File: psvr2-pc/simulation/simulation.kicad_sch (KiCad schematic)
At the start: 32 parts, among them Q1 PMOS, Q2 PMOS, Q3 NPN, Q4 PMOS, Q5 PMOS, Q6 NPN, Q8 PMOS

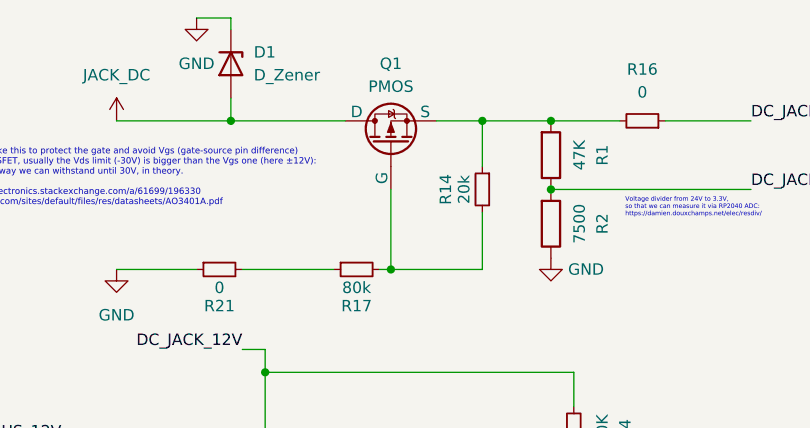
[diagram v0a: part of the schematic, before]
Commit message: Start to learn how to add the SPICE model parameters to simulate a TVS voltage protection diode array and confirm it works, not working yet, getting there.
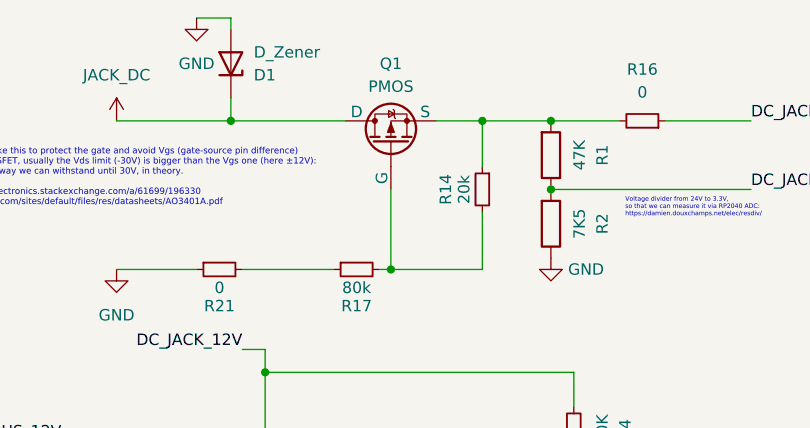
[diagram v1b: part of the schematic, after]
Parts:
- R2: value 7500 -> 7K5
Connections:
- net GND: now also D1.2 (A); no longer D1.1 (K)
- net JACK_DC: now also D1.1 (K); no longer D1.2 (A)
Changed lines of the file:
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@@
 			)
 		)
-		(property "Value" "7500"
+		(property "Value" "7K5"
 			(at 120.015 33.02 90)
 			(effects
@@
 		(lib_id "Device:D_Zener")
 		(at 81.28 15.24 270)
-		(unit 1)
-		(exclude_from_sim no)
-		(in_bom yes)
-		(on_board yes)
-		(dnp no)
-		(fields_autoplaced yes)
+		(mirror x)
+		(unit 1)
+		(exclude_from_sim no)
+		(in_bom yes)
+		(on_board yes)
+		(dnp no)
 		(property "Reference" "D1"
-			(at 83.82 13.9699 90)
+			(at 83.82 16.5101 90)
 			(effects
 				(font
@@
 		)
 		(property "Value" "D_Zener"
-			(at 83.82 16.5099 90)
+			(at 83.82 13.9701 90)
 			(effects
 				(font
@@
 			)
 		)
-		(property "Datasheet" "~"
+		(property "Datasheet" "https://protekdevices.com/wp-content/uploads/datasheets/psm712.pdf"
 			(at 81.28 15.24 0)
 			(effects
@@
 			)
 		)
-		(property "Description" "Zener diode"
+		(property "Description" "TVS ARRAY"
 			(at 81.28 15.24 0)
 			(effects
@@
 			)
 		)
-		(property "Sim.Pins" "1=K, 2=A"
+		(property "Sim.Pins" "1=A 2=K"
 			(at 81.28 15.24 0)
 			(effects
+				(font
+					(size 1.27 1.27)
+				)
+				(hide yes)
+			)
+		)
+		(property "Sim.Params" "m=0.33 is=1e-13 rs=0.40 n=1 tt=1E vj=.6 cjp=1.23e-10 eg=1.11 bv=13.3 ibv=0.001"
+			(at 81.28 15.24 0)
+			(effects

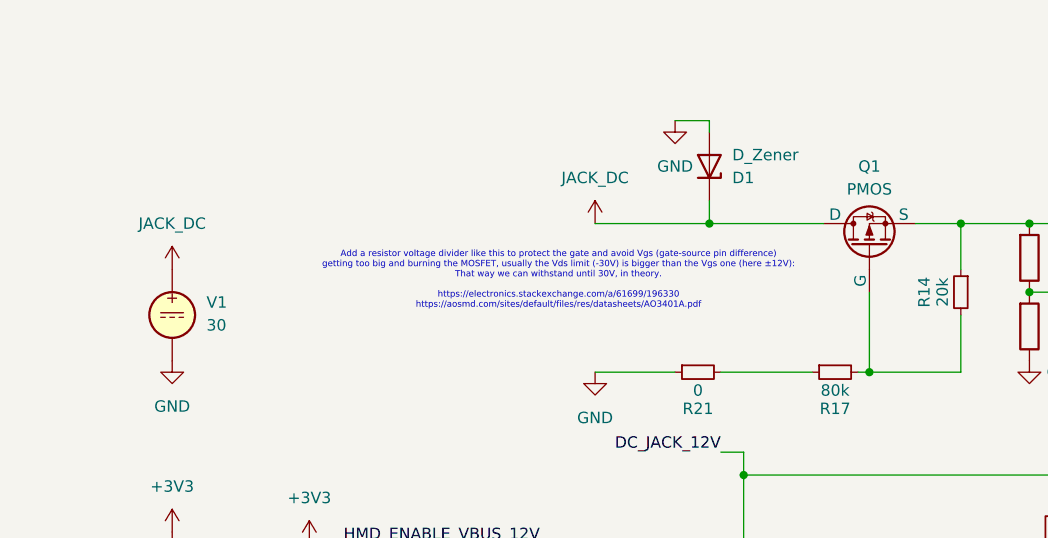
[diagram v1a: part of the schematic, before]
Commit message: Mess around a bit more with the simulation. can't say I really know what's wrong or why the simulation isn't clamping anything. Worth studying more in the future.
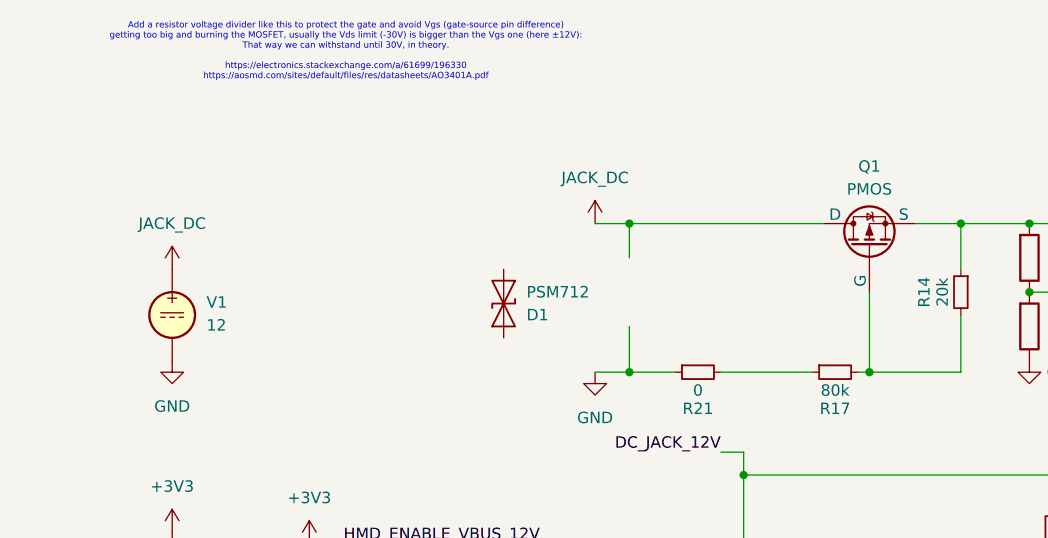
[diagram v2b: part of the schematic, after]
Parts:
- removed D1: D_Zener, symbol Device:D_Zener
- added D1: PSM712, Diode_SMD:D_SMA, symbol Diode:SMAJ12CA
- V1: value 30 -> 12

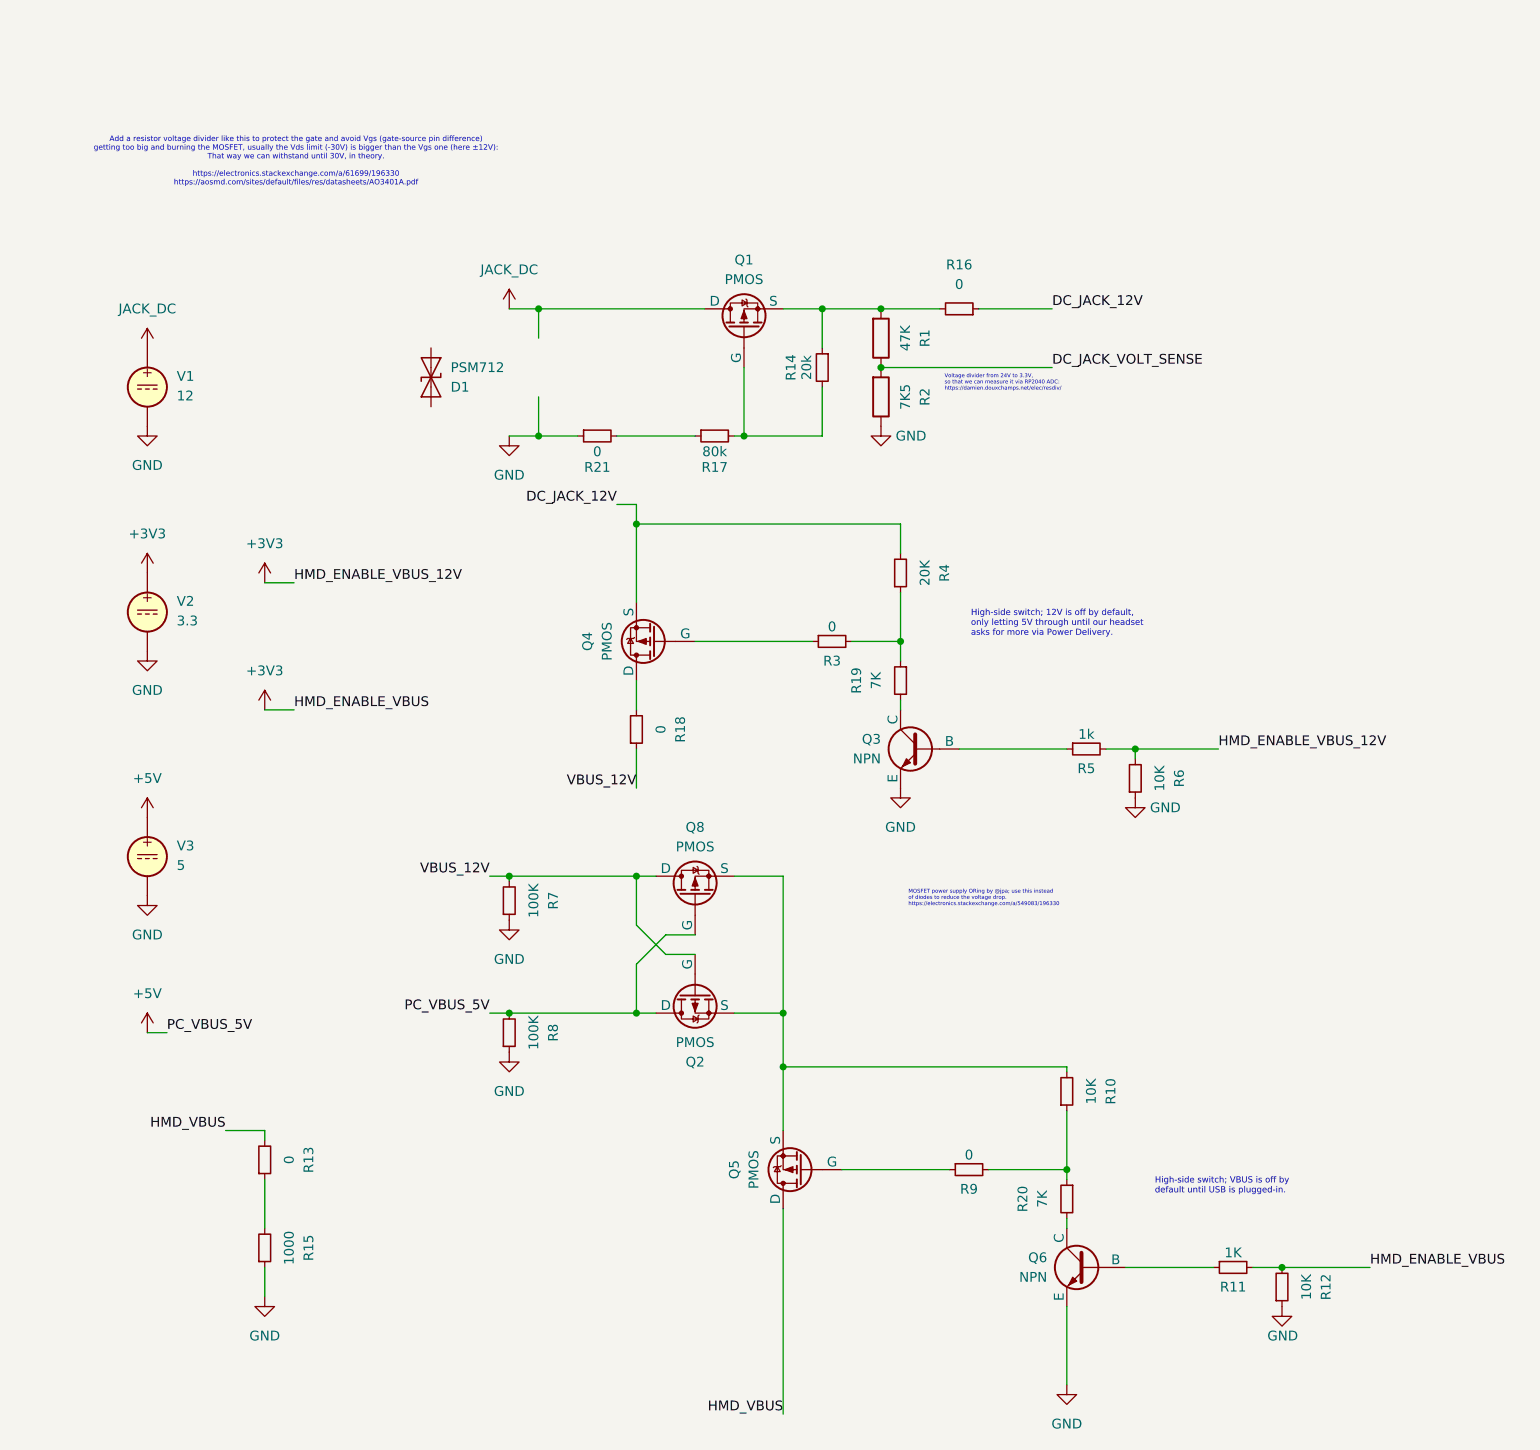
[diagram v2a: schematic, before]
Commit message: Fix the power gating simulation again, remove all the custom properties and impedance from the 12V power source. Switch from the generic NPN transistors to MMBT2222A.
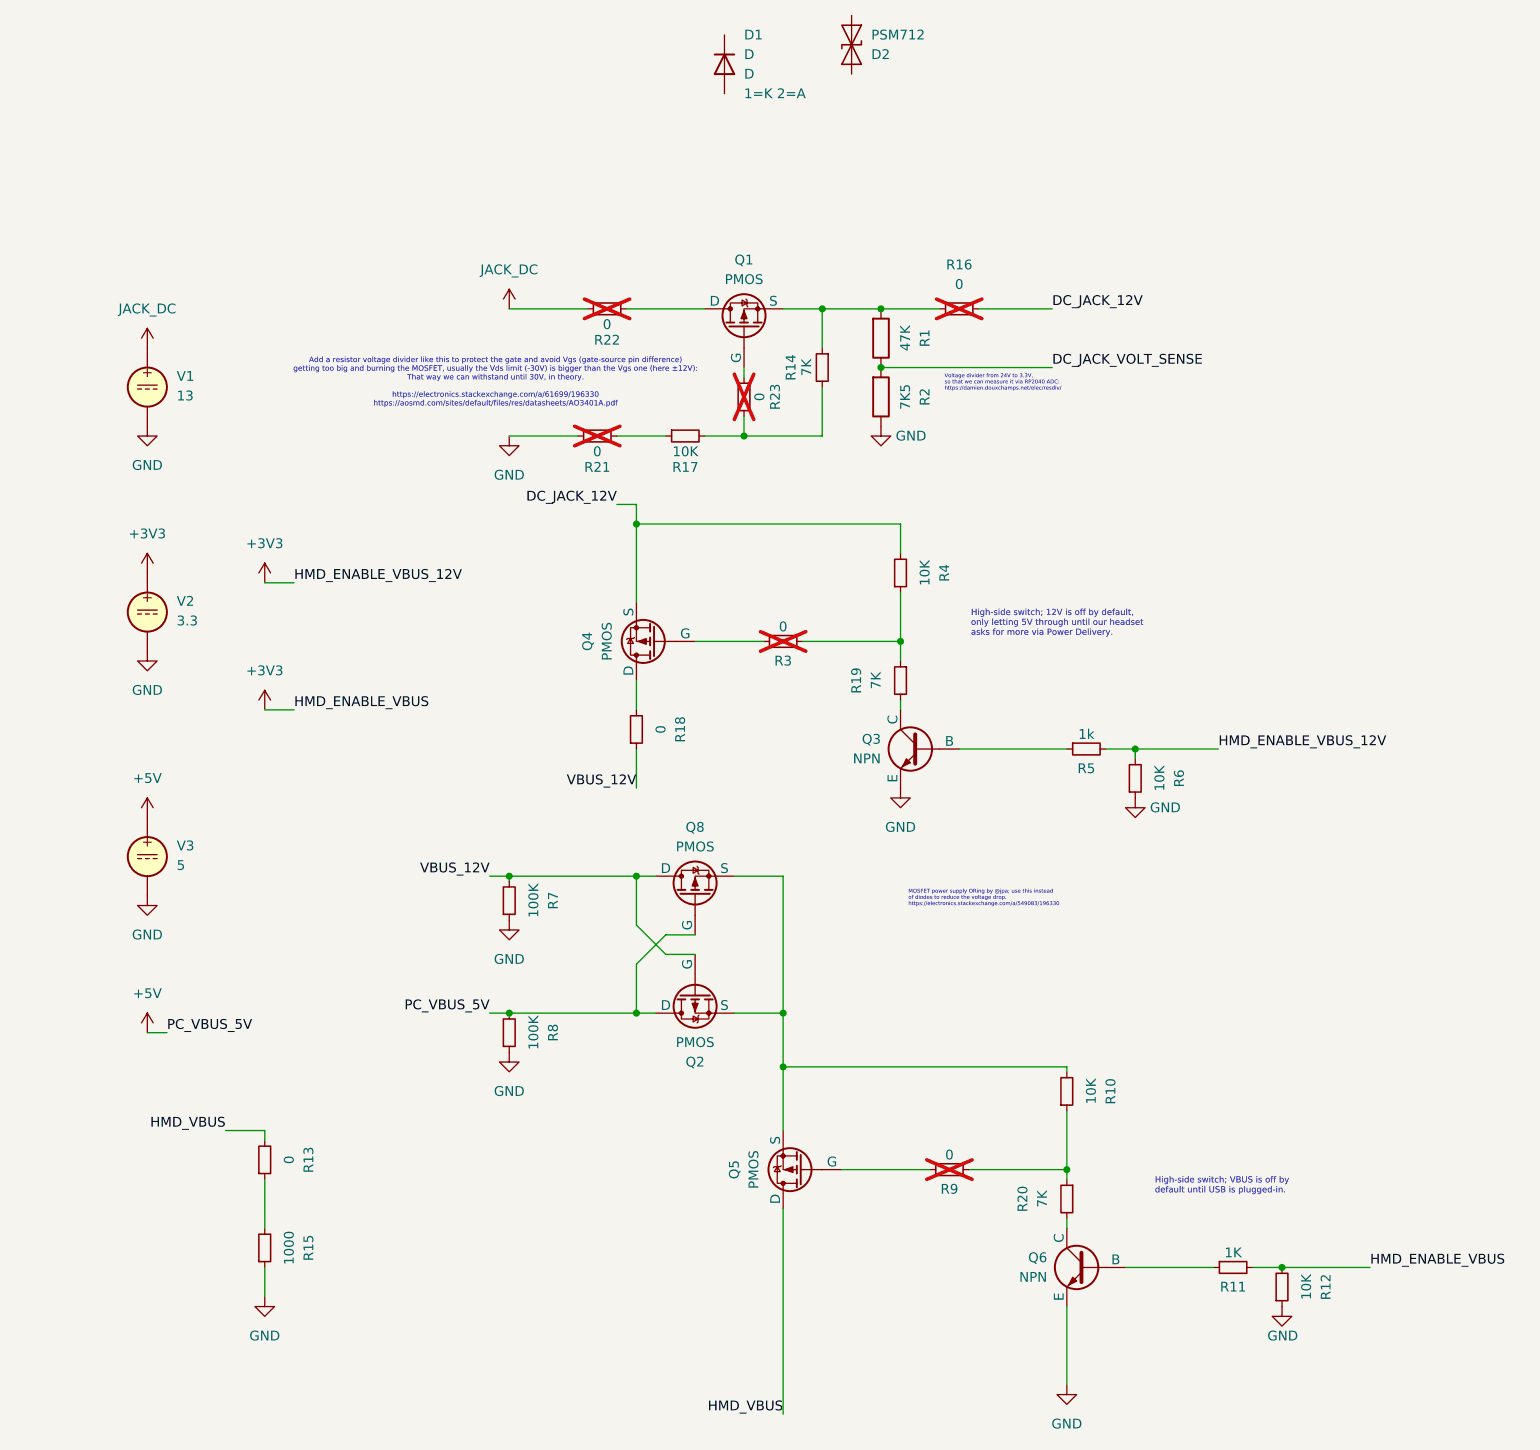
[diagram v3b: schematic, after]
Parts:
- removed D1: PSM712, Diode_SMD:D_SMA, symbol Diode:SMAJ12CA
- added D1: D, symbol Simulation_SPICE:D
- added D2: PSM712, Diode_SMD:D_SMA, symbol Diode:SMAJ12CA
- added R22, R23: 0, Resistor_SMD:R_0805_2012Metric, symbol Device:R_Small
- R14: value 20k -> 7K
- R16, R21, R3, R9: now not fitted
- R17: value 80k -> 10K
- R4: value 20K -> 10K
- V1: value 12 -> 13
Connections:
- net JACK_DC: now also R22.1; no longer Q1.1 (D)
- net at R14.2, R17.2: now also R23.1; no longer Q1.2 (G)
- new net: Q1.1 (D), R22.2
- new net: Q1.2 (G), R23.2
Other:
- moved on the sheet: R17

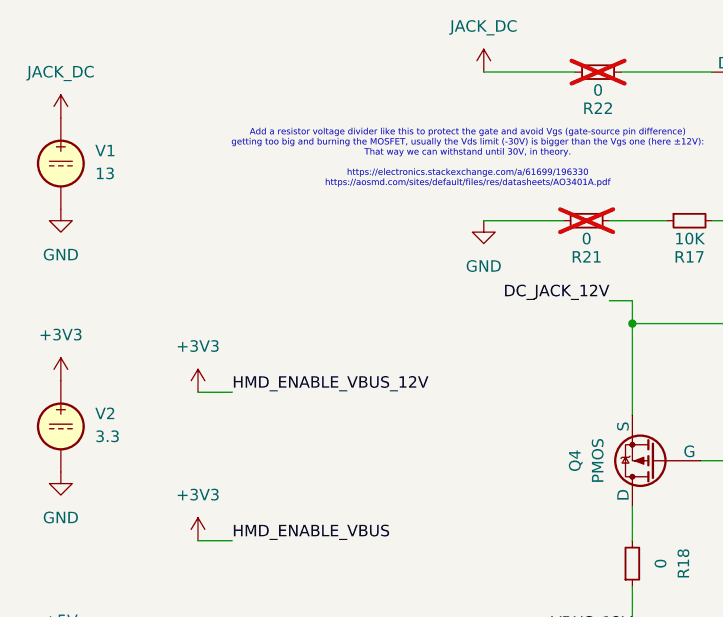
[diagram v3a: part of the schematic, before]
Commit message: Use relative paths for the SPICE symbols, store them in the git repository. Just to make things easier. Explain how to toggle pins, for those struggling like me.
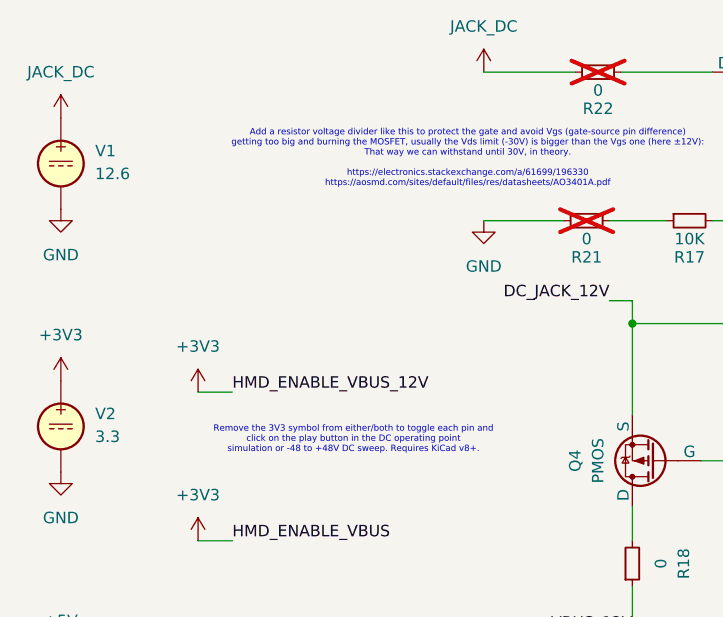
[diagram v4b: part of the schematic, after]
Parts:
- V1: value 13 -> 12.6
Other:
- note added: "Remove the 3V3 symbol from either/both to toggle each pin and click on the play button in the DC operating point simulation or -48 to +48V DC sweep. Requires KiCad v8+."
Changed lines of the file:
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@@
 		)
 	)
+	(text "Remove the 3V3 symbol from either/both to toggle each pin and\nclick on the play button in the DC operating point\nsimulation or -48 to +48V DC sweep. Requires KiCad v8+."
+		(exclude_from_sim no)
+		(at 54.102 62.484 0)
+		(effects
+			(font
+				(size 0.7 0.7)
+			)
+		)
+	)
 	(text "Voltage divider from 24V to 3.3V,\nso that we can measure it via RP2040 ADC:\nhttps://damien.douxchamps.net/elec/resdiv/"
 		(exclude_from_sim no)
@@
 			)
 		)
-		(property "Value" "13"
+		(property "Value" "12.6"
 			(at 25.4 32.8901 0)
 			(effects
@@
 			)
 		)
-		(property "Sim.Library" "C:\\Users\\Usuario\\Downloads\\MMBT2222A.txt"
+		(property "Sim.Library" "./_spice_component_models/MMBT2222A.txt"
 			(at 143.51 146.05 0)
 			(effects
@@
 			)
 		)
-		(property "Sim.Library" "C:\\Users\\Usuario\\Downloads\\AO3401A.mod"
+		(property "Sim.Library" "./_spice_component_models/AO3401A.mod"
 			(at 106.68 133.35 0)
 			(effects
@@
 			)
 		)
-		(property "Sim.Library" "C:\\Users\\Usuario\\Downloads\\AO3401A.mod"
+		(property "Sim.Library" "./_spice_component_models/AO3401A.mod"
 			(at 92.71 97.79 90)
 			(effects
@@
 			)
 		)
-		(property "Sim.Library" "C:\\Users\\Usuario\\Downloads\\AO3401A.mod"
+		(property "Sim.Library" "./_spice_component_models/AO3401A.mod"
 			(at 87.63 64.77 0)
 			(effects
@@
 			)
 		)
-		(property "Sim.Library" "C:\\Users\\Usuario\\Downloads\\MMBT2222A.txt"
+		(property "Sim.Library" "./_spice_component_models/MMBT2222A.txt"
 			(at 121.92 78.74 0)
 			(effects
@@
 			)
 		)
-		(property "Sim.Library" "C:\\Users\\Usuario\\Downloads\\AO3401A.mod"
+		(property "Sim.Library" "./_spice_component_models/AO3401A.mod"
 			(at 99.06 24.13 0)
 			(effects
@@
 			)
 		)
-		(property "Sim.Library" "C:\\Users\\Usuario\\Downloads\\AO3401A.mod"
+		(property "Sim.Library" "./_spice_component_models/AO3401A.mod"
 			(at 92.71 110.49 0)
 			(effects

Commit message: Update the resistor sizes to make them cheap. Use 51K/8K2 for the 24V to 3.3V divider. Use 6K8 instead of 7K. Update the simulation, seems to still work fine. Add the LCSC Part # to the NPN transistor and remove obsolete C part numbers from resistors and capacitors that now had the wrong size. Mark the M4 and SMT assembly holes as not-in-schematic and not in position file, name them to avoid auto-generated names which cause errors in  the JLC ordering process.
Currently available resistor sizes as basic parts:
5.1kΩ 6.8kΩ 8.2kΩ
47kΩ 51kΩ 68kΩ
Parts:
- R1: value 47K -> 51K
- R14, R19, R20: value 7K -> 6K8
- R2: value 7K5 -> 8K2
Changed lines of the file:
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@@
 			)
 		)
-		(property "Value" "7K5"
+		(property "Value" "8K2"
 			(at 120.015 33.02 90)
 			(effects
@@
 			)
 		)
-		(property "Value" "7K"
+		(property "Value" "6K8"
 			(at 107.188 29.21 90)
 			(effects
@@
 			)
 		)
-		(property "Value" "7K"
+		(property "Value" "6K8"
 			(at 137.795 137.16 90)
 			(effects
@@
 			)
 		)
-		(property "Value" "47K"
+		(property "Value" "51K"
 			(at 120.015 25.4 90)
 			(effects
@@
 			)
 		)
-		(property "Value" "7K"
+		(property "Value" "6K8"
 			(at 116.205 69.85 90)
 			(effects
